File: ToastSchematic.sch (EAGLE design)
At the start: 88 parts, among them Q1 DMN63D8LDW, Q2 DMN63D8LDW, Q3 DMN63D8LDW, Q4 DMN63D8LDW, T1 BPX81, T2 BPX81, T3 BPX81, T4 BPX81, T5 BPX81, T6 BPX81, U3 DRV8839_DSS_12, U4 DRV8839_DSS_12, X1 22-23-2021, X2 22-23-2021, X3 22-23-2021, X4 22-23-2021, X5 22-23-2021, X6 22-23-2021

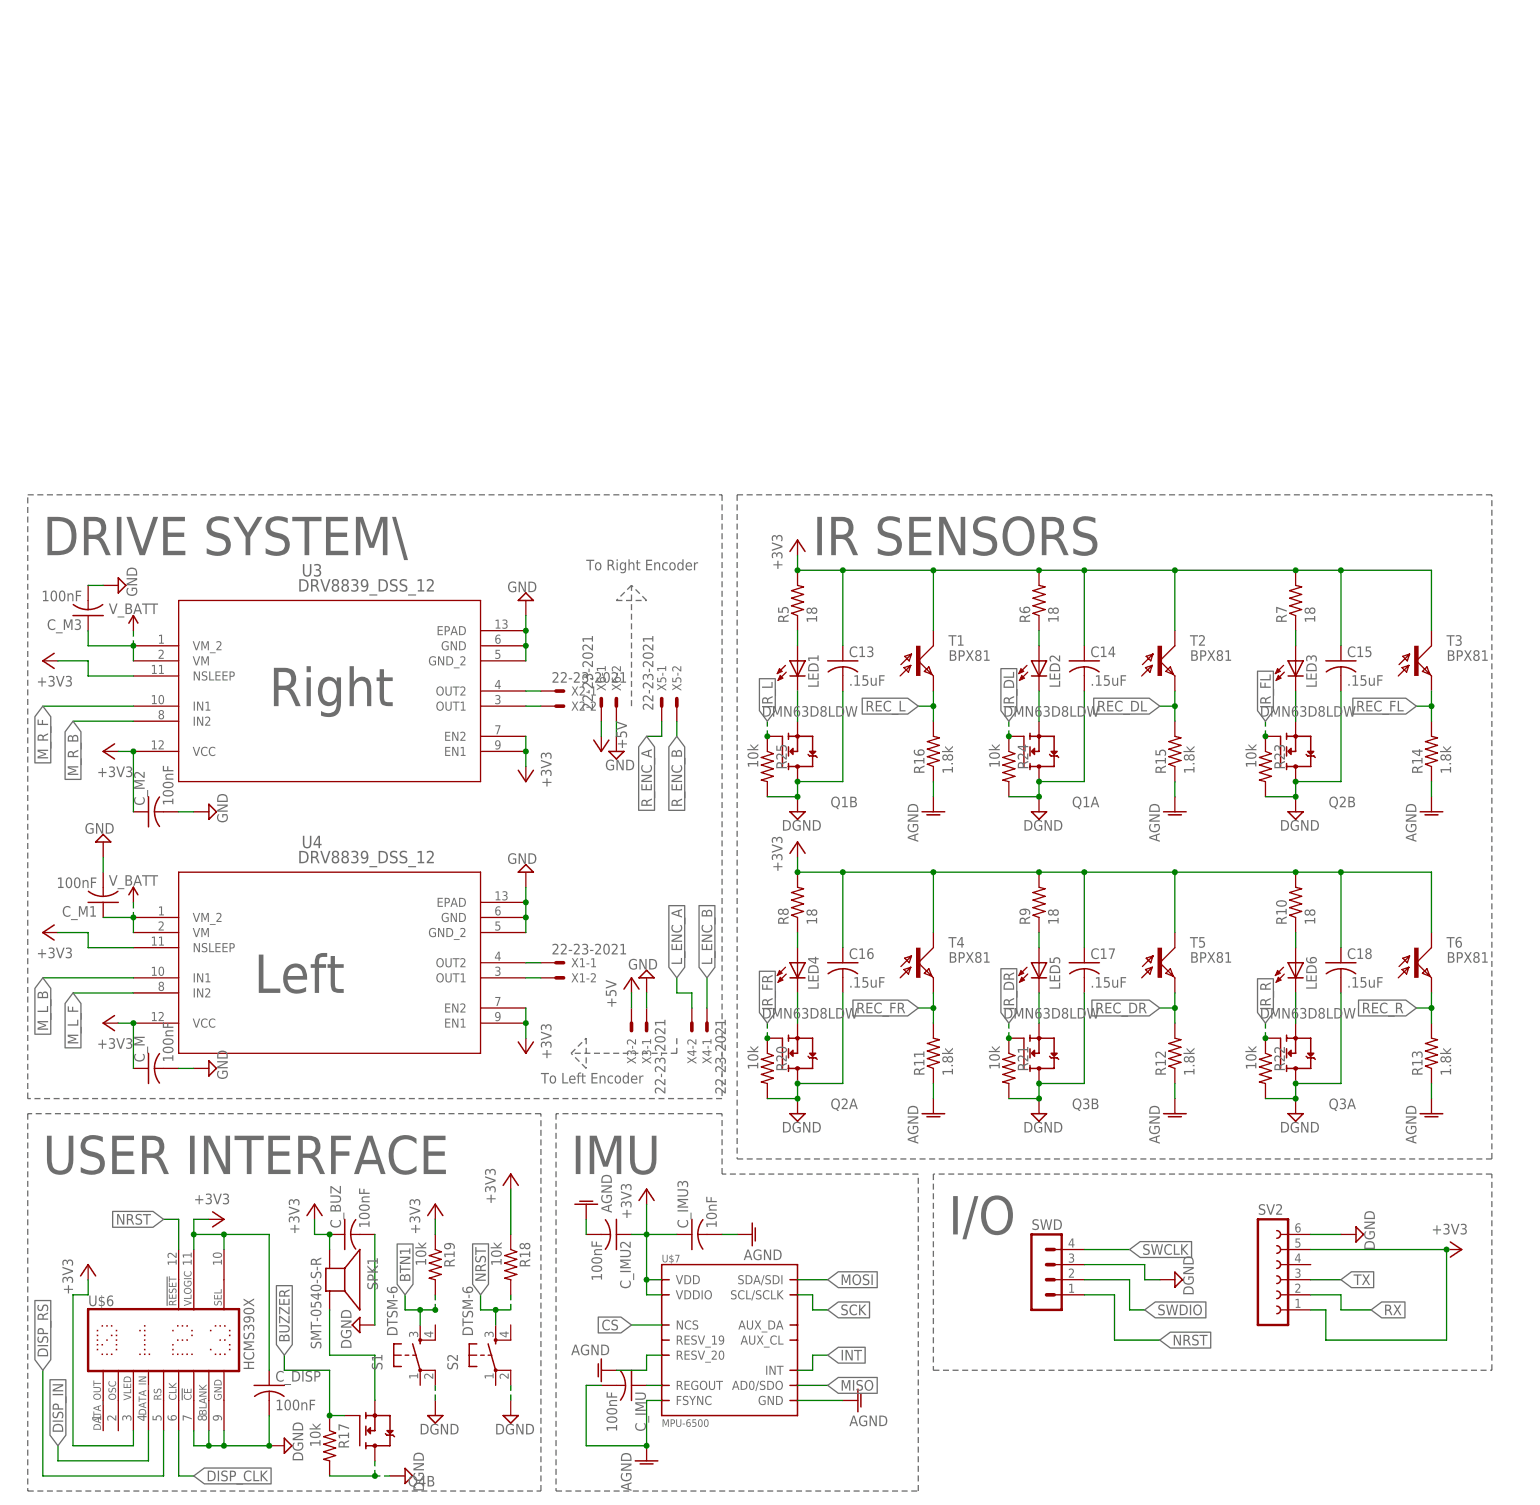
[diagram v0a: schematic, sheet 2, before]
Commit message: started pcb board layout
put parts where they should be
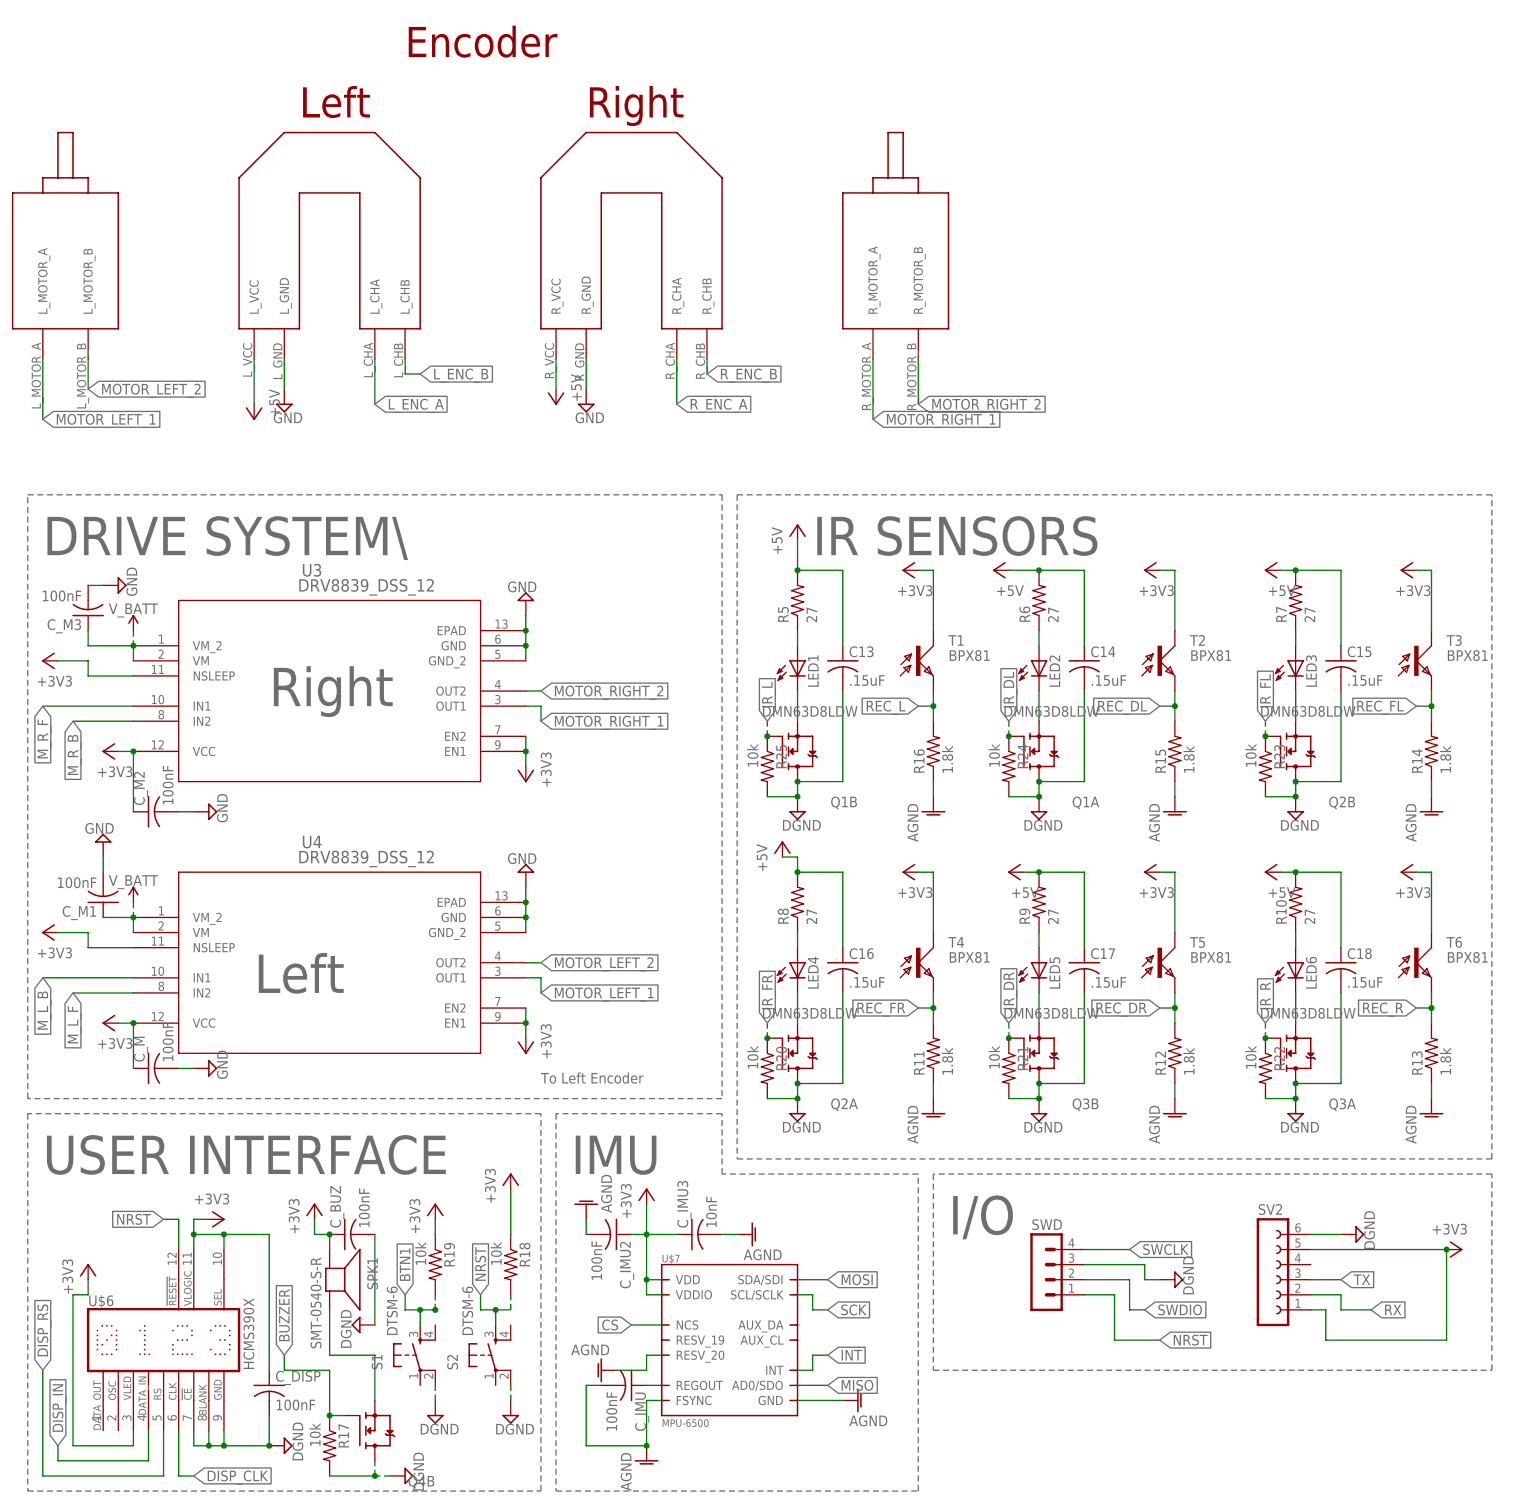
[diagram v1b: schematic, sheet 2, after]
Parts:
- removed X1, X2, X3, X4, X5, X6: 22-23-2021, con-molex:22-23-2021
- added U$4: FUTURA_V1.0_MOTOR_MOUNT, Futura 1.0 motor mount template:FUTURA_V1.0_MOTOR_MOUNT
- R10, R5, R6, R7, R8, R9: value 18 -> 27
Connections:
- removed net N$3: U3.OUT2, X2-1.S
- removed net N$4: U3.OUT1, X2-2.S
- removed net N$7: U4.OUT2, X1-1.S
- removed net N$8: U4.OUT1, X1-2.S
- new net MOTOR_LEFT_1: U$4.L_MOTOR_A, U4.OUT1
- new net MOTOR_LEFT_2: U$4.L_MOTOR_B, U4.OUT2
- new net MOTOR_RIGHT_1: U$4.R_MOTOR_A, U3.OUT1
- new net MOTOR_RIGHT_2: U$4.R_MOTOR_B, U3.OUT2
- net +3V3: no longer C13.1, C14.1, C15.1, C16.1, C17.1, C18.1, R10.2, R5.2, R6.2, R7.2, R8.2, R9.2
- net +5V: now also C13.1, C14.1, C15.1, C16.1, C17.1, C18.1, R10.2, R5.2, R6.2, R7.2, R8.2, R9.2, U$4.L_VCC, U$4.R_VCC; no longer X3-2.S, X6-1.S
- net GND: now also U$4.L_GND, U$4.R_GND; no longer X3-1.S, X6-2.S
- net L_ENC_A: now also U$4.L_CHA; no longer X4-2.S
- net L_ENC_B: now also U$4.L_CHB; no longer X4-1.S
- net R_ENC_A: now also U$4.R_CHA; no longer X5-1.S
- net R_ENC_B: now also U$4.R_CHB; no longer X5-2.S
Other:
- note removed: "To Right Encoder"

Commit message: added gnd plane
added gnd plane
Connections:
- net DGND: now also U$4.L_GND, U$4.R_GND
- net GND: no longer U$4.L_GND, U$4.R_GND
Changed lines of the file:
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@@
 <part name="U4" library="DRV8839" deviceset="DRV8839_DSS_12" device=""/>
 <part name="SUPPLY17" library="SparkFun-PowerSymbols" deviceset="V_BATT" device=""/>
-<part name="SUPPLY18" library="supply2" library_urn="urn:adsk.eagle:library:372" deviceset="GND" device=""/>
 <part name="SUPPLY19" library="supply2" library_urn="urn:adsk.eagle:library:372" deviceset="GND" device=""/>
 <part name="SUPPLY20" library="supply2" library_urn="urn:adsk.eagle:library:372" deviceset="GND" device=""/>
@@
 <part name="P+4" library="supply1" library_urn="urn:adsk.eagle:library:371" deviceset="+5V" device=""/>
 <part name="P+5" library="supply1" library_urn="urn:adsk.eagle:library:371" deviceset="+5V" device=""/>
-<part name="SUPPLY14" library="supply2" library_urn="urn:adsk.eagle:library:372" deviceset="GND" device=""/>
 <part name="SV2" library="con-lsta" library_urn="urn:adsk.eagle:library:161" deviceset="FE06-1" device="" package3d_urn="urn:adsk.eagle:package:8191/1"/>
 <part name="+3V21" library="supply1" library_urn="urn:adsk.eagle:library:371" deviceset="+3V3" device=""/>
@@
 <part name="+3V24" library="supply1" library_urn="urn:adsk.eagle:library:371" deviceset="+3V3" device=""/>
 <part name="+3V25" library="supply1" library_urn="urn:adsk.eagle:library:371" deviceset="+3V3" device=""/>
+<part name="SUPPLY14" library="supply2" library_urn="urn:adsk.eagle:library:372" deviceset="DGND" device=""/>
+<part name="SUPPLY18" library="supply2" library_urn="urn:adsk.eagle:library:372" deviceset="DGND" device=""/>
 </parts>
 <sheets>
@@
 <instance part="U4" gate="A" x="25.4" y="101.6"/>
 <instance part="SUPPLY17" gate="G$1" x="25.4" y="149.86"/>
-<instance part="SUPPLY18" gate="GND" x="101.6" y="187.96"/>
 <instance part="SUPPLY19" gate="GND" x="91.44" y="154.94" rot="R180"/>
 <instance part="SUPPLY20" gate="GND" x="91.44" y="109.22" rot="R180"/>
@@
 <instance part="P+4" gate="1" x="96.52" y="187.96" rot="R180"/>
 <instance part="P+5" gate="1" x="45.72" y="185.42" rot="R180"/>
-<instance part="SUPPLY14" gate="GND" x="50.8" y="187.96"/>
 <instance part="SV2" gate="G$1" x="215.9" y="40.64"/>
 <instance part="+3V21" gate="G$1" x="248.92" y="45.72" rot="R270"/>
@@
 <instance part="+3V24" gate="G$1" x="238.76" y="109.22" rot="R90"/>
 <instance part="+3V25" gate="G$1" x="238.76" y="160.02" rot="R90"/>
+<instance part="SUPPLY14" gate="G$1" x="50.8" y="185.42"/>
+<instance part="SUPPLY18" gate="G$1" x="101.6" y="185.42"/>
 </instances>
 <busses>
@@
 <pinref part="SUPPLY39" gate="GND" pin="GND"/>
 <wire x1="33.02" y1="119.38" x2="35.56" y2="119.38" width="0.1524" layer="91"/>
-</segment>
-<segment>
-<pinref part="SUPPLY14" gate="GND" pin="GND"/>
-<pinref part="U$4" gate="G$1" pin="L_GND"/>
-<wire x1="50.8" y1="195.58" x2="50.8" y2="190.5" width="0.1524" layer="91"/>
-</segment>
-<segment>
-<pinref part="SUPPLY18" gate="GND" pin="GND"/>
-<pinref part="U$4" gate="G$1" pin="R_GND"/>
-<wire x1="101.6" y1="190.5" x2="101.6" y2="195.58" width="0.1524" layer="91"/>
 </segment>
 </net>
@@
 <wire x1="66.04" y1="48.26" x2="66.04" y2="33.02" width="0.1524" layer="91"/>
 </segment>
-</net>
+<segment>
+<pinref part="U$4" gate="G$1" pin="L_GND"/>
+<wire x1="50.8" y1="195.58" x2="50.8" y2="193.04" width="0.1524" layer="91"/>
+<pinref part="SUPPLY14" gate="G$1" pin="DGND"/>
+<wire x1="50.8" y1="193.04" x2="50.8" y2="190.5" width="0.1524" layer="91"/>
+<wire x1="50.8" y1="187.96" x2="50.8" y2="190.5" width="0.1524" layer="91"/>
+</segment>
+<segment>
+<pinref part="U$4" gate="G$1" pin="R_GND"/>
+<wire x1="101.6" y1="190.5" x2="101.6" y2="193.04" width="0.1524" layer="91"/>
+<pinref part="SUPPLY18" gate="G$1" pin="DGND"/>
+<wire x1="101.6" y1="193.04" x2="101.6" y2="195.58" width="0.1524" layer="91"/>
+<wire x1="101.6" y1="187.96" x2="101.6" y2="190.5" width="0.1524" layer="91"/>
+</segment>
+</net>
